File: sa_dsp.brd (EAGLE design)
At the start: 150 x 110 mm, 409 parts, among them CN1 uSD, CN2 MINI B USB, CN3 2X5 HEADER, CN4 MINI B USB, CN5 USB A, CN6 MINI B USB, Q1 2N7002, Q2 2N7002, Q3 2N7002, Q4 2N7002, SW1 1825910-7, U1 PGA2311, U10 LME49720, U11 PGA2311, U12 LME49720, U13 LME49720, U14 PCM1754, U15 LME49720, U16 PGA2311, U17 LME49720, U18 LME49720, U19 PCM1754, U2 LM317, U20 LME49720, U21 7 SEG, U22 74HC164A, U23 PCM2707, U24 PCM2707, U25 7 SEG, U26 74HC164A, U27 LM337, U28 LM317, U29 7 SEG, U3 OSD3358-512M-BSM, U30 74HC164A, U31 100MHz, U32 USBLC6-2SC6, U33 FT230X, U34 USBLC6-2SC6, U35 USBLC6-2SC6, U36 USBLC6-2SC6, U37 2 PORT HUB, U38 TPS70925, U39 LM22670, U4 LME49720, U40 MPM3820, U41 MPM3820, U5 LME49720, U6 10CL016YF484C6G, U7 7 SEG, U8 74HC164A, U9 PCM1754

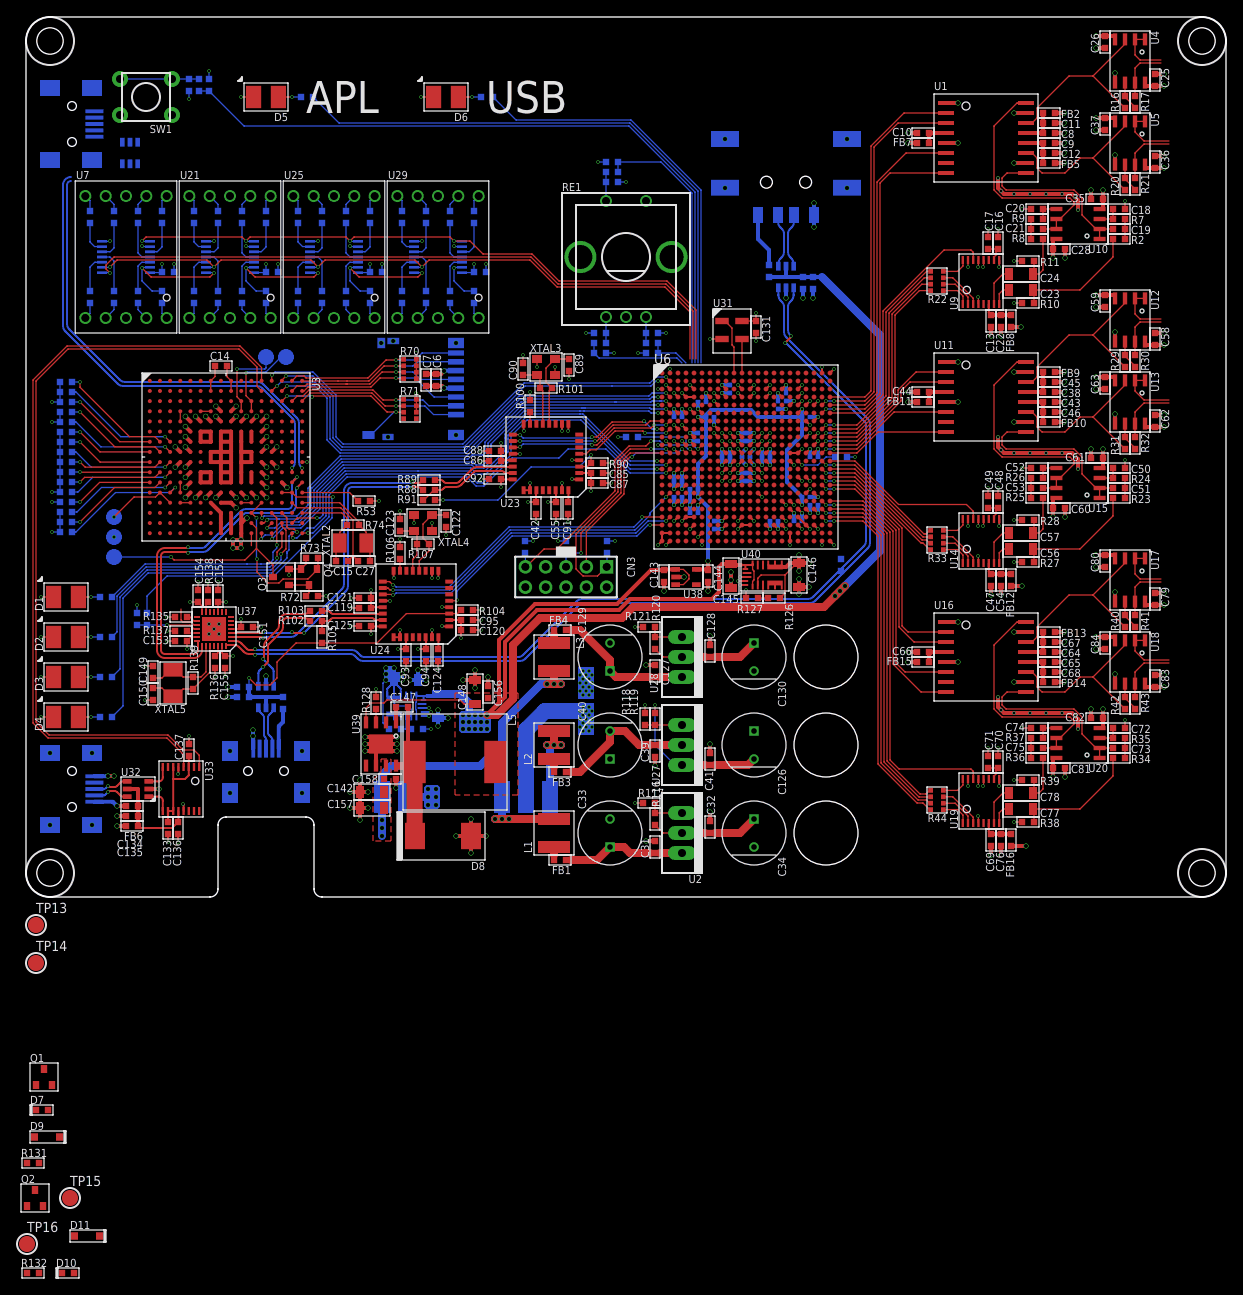
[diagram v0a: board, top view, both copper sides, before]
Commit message: FPGA config needs check, full review, DRC, airwires and architecture review needed
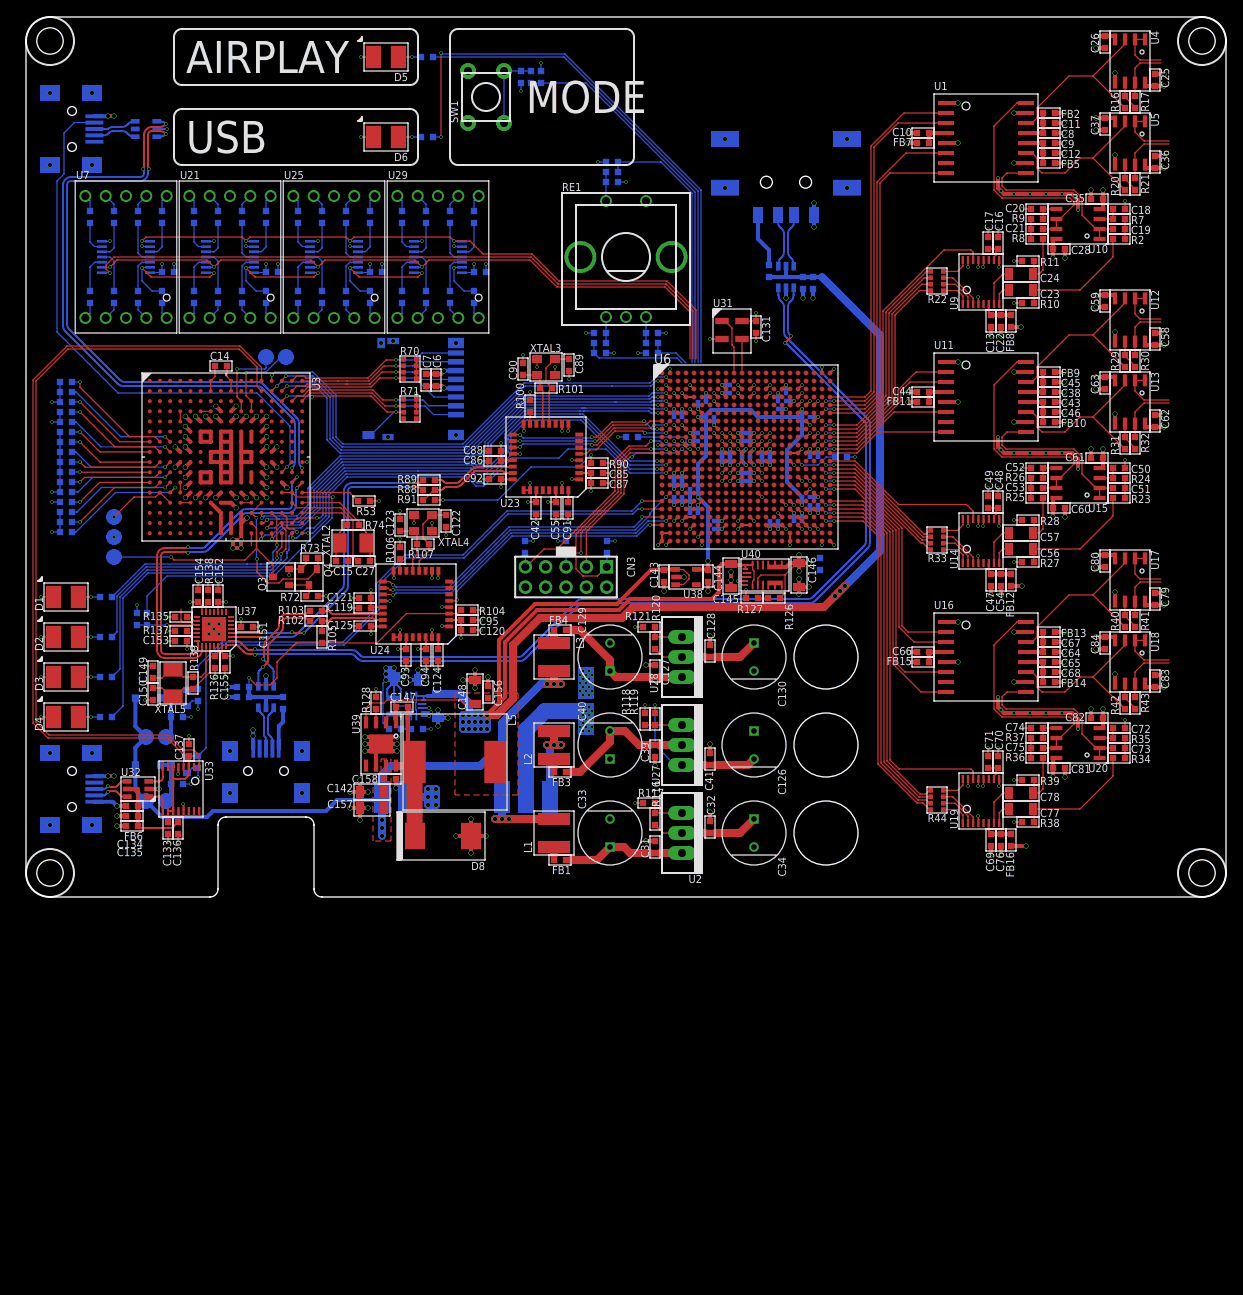
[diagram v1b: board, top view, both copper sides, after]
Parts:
- moved R132 75.1 mm to (21.5, 25.2), flipped to the bottom, turned to 90 degrees
- moved D10 70.8 mm to (18.9, 22.5), flipped to the bottom, turned to 180 degrees
- moved D11 67.7 mm to (15.2, 24.9), flipped to the bottom
- moved TP16 65.7 mm to (17.5, 20.0), flipped to the bottom, turned to 270 degrees
- moved Q2 65.0 mm to (19.1, 24.9), flipped to the bottom, turned to 270 degrees
- moved TP15 58.4 mm to (15.0, 20.0), flipped to the bottom, turned to 270 degrees
- moved R131 54.2 mm to (21.5, 16.9), flipped to the bottom, turned to 90 degrees
- moved D9 48.2 mm to (15.2, 16.5), flipped to the bottom
- moved D7 44.1 mm to (18.9, 14.1), flipped to the bottom, turned to 180 degrees
- moved SW1 42.5 mm to (57.5, 100.0), turned to 90 degrees
- moved Q1 42.5 mm to (19.1, 16.5), flipped to the bottom, turned to 270 degrees
- moved C132 41.5 mm to (64.4, 102.5)
- moved R122 41.5 mm to (61.9, 102.5)
- moved R123 41.5 mm to (63.1, 102.5)
- moved TP14 26.0 mm to (17.5, 12.0), flipped to the bottom, turned to 270 degrees
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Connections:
- net IO_AUDIO_RLY_EN: now also U6.U1
- net PSU_AMP_PWR_EN: now also U6.V1
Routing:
- net PSU_AMP_PWR_EN: track 0.00 -> 80.3 mm, vias 0 -> 1
- net IO_AUDIO_RLY_EN: track 0.00 -> 72.7 mm, vias 0 -> 1
- net OSD_DEBUG_USB_ID: track 0.00 -> 69.8 mm, vias 0 -> 1
- net 15VD_UNREG: track 39.6 -> 85.5 mm
- net UI_INPUT_SEL: track 88.6 -> 47.5 mm
- net UI_INPUT_USB: track 52.4 -> 72.7 mm, vias 0 -> 2
- net OSD_DEBUG_USB_DM: track 58.6 -> 77.3 mm, vias 1 -> 3
- net OSD_DEBUG_USB_DP: track 59.4 -> 78.0 mm, vias 1 -> 3
- net UI_INPUT_AIRPLAY: track 74.5 -> 61.6 mm
- net GND: track 337.1 -> 349.0 mm, vias 315 -> 326
- net N$237: track 0.00 -> 6.43 mm
- net N$207: track 0.00 -> 6.06 mm
- net N$209: track 0.00 -> 5.37 mm
- net N$208: track 0.00 -> 5.31 mm
- net 3V3: track 153.7 -> 154.9 mm
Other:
- board text added: "AIRPLAY"
- board text added: "MODE"
- board text removed: "APL"

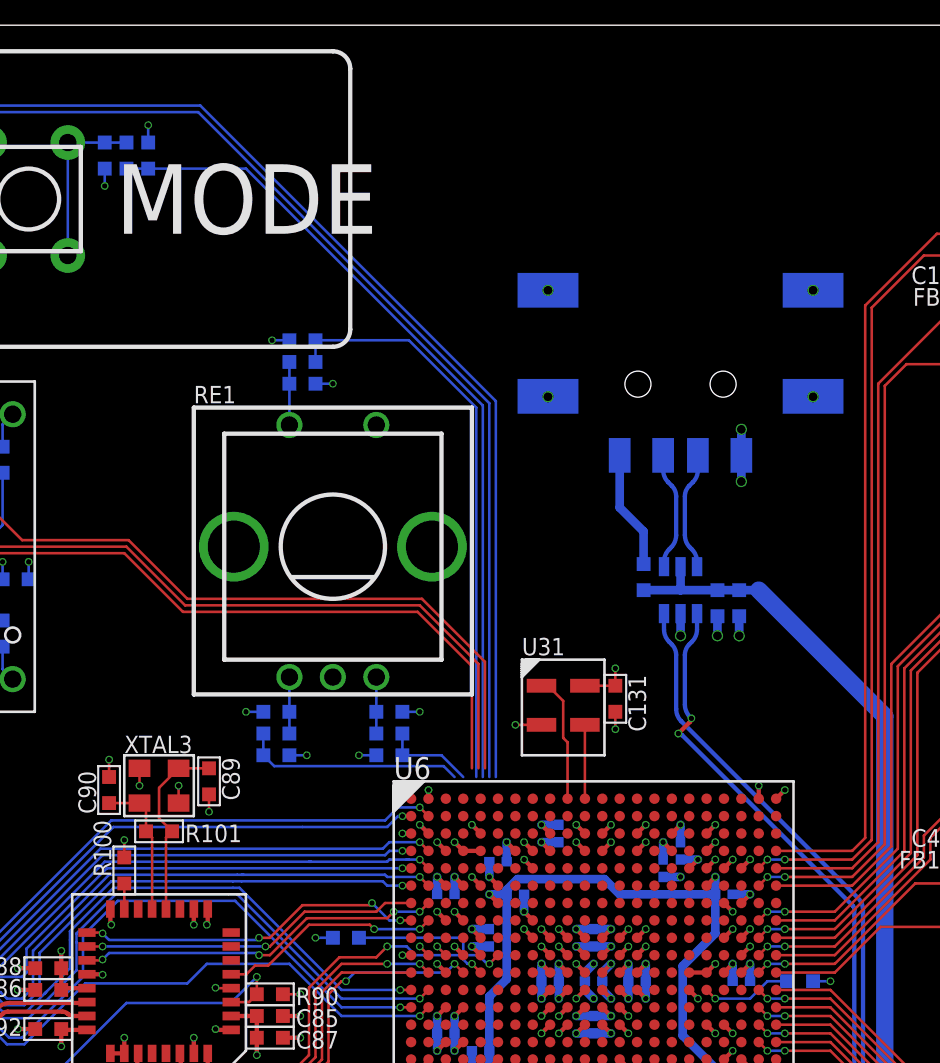
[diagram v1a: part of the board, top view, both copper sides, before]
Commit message: Schmit triggers done, FPGA conf done
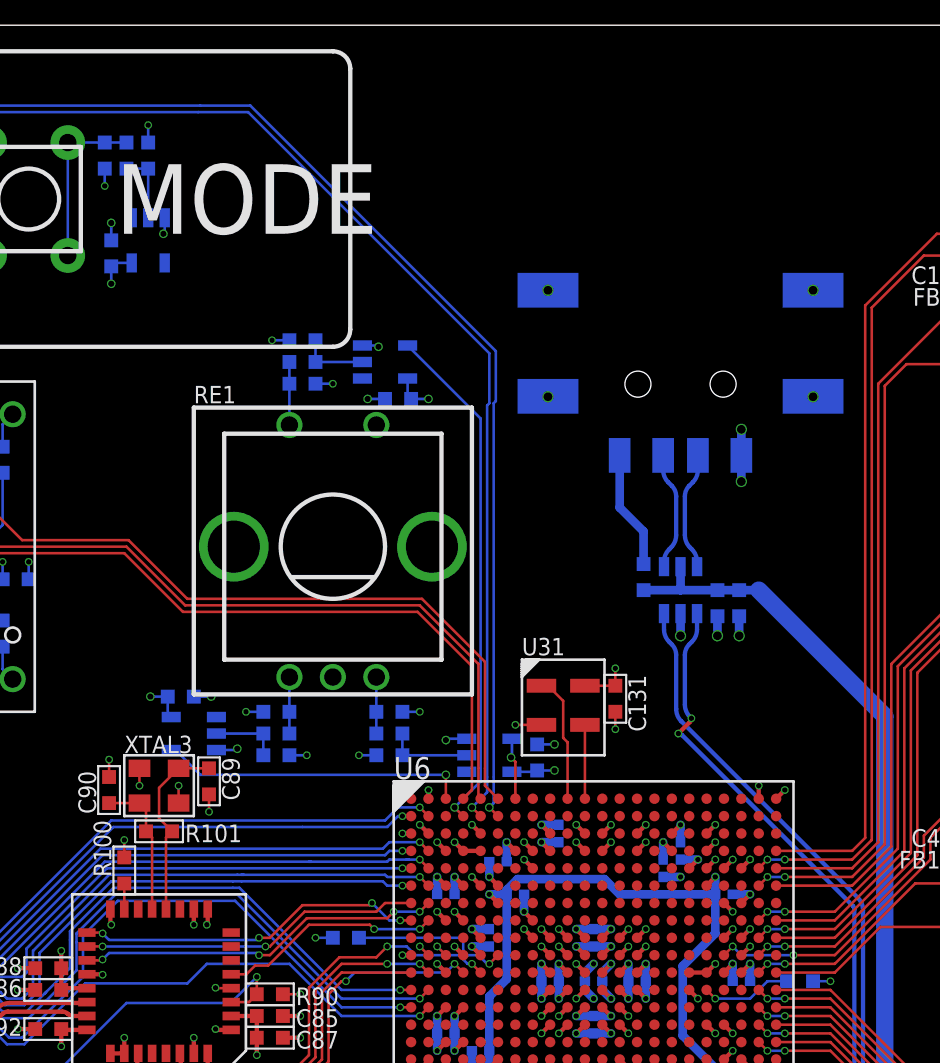
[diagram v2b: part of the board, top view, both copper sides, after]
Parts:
- added C161, C162, C163, C164: 100nF 16V, CAPACITORS:0603
- added U42, U43, U44, U45: SN74LVC1G17D, ICs:SOT23-5
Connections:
- new net N$238: C4.2, R5.2, U43.2
- new net N$239: C1.2, R4.2, U42.2
- new net N$240: C29.2, R13.1, U44.2
- new net N$241: C132.2, R123.2, U45.2
- net 3V3: now also C161.2, C162.2, C163.2, C164.2, U42.5, U43.5, U44.5, U45.5
- net DISP_SPI_!CE: now also U6.A4
- net DISP_SPI_MOSI: now also U6.A5
- net DISP_SPI_SCLK: now also U6.A6
- net ENC_A: now also U42.4, U6.A3; no longer C1.2, R4.2
- net ENC_B: now also U43.4, U6.A7; no longer C4.2, R5.2
- net ENC_SW: now also U44.4, U6.B4; no longer C29.2, R13.1
- net GND: now also C161.1, C162.1, C163.1, C164.1, U42.3, U43.3, U44.3, U45.3
- net PGA1_SDI: now also U6.K19; no longer U6.K22
- net UI_INPUT_AIRPLAY: now also U6.B5
- net UI_INPUT_SEL: now also U45.4; no longer C132.2, R123.2
- net UI_INPUT_USB: now also U6.B6
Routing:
- net UI_INPUT_SEL: track 47.5 -> 0.00 mm
- net 3V3: track 154.9 -> 164.1 mm, vias 82 -> 86
- net GND: track 349.0 -> 357.3 mm, vias 326 -> 334
- net ENC_A: track 12.8 -> 17.8 mm, vias 0 -> 1
- net N$238: track 0.00 -> 4.95 mm
- net UI_INPUT_AIRPLAY: track 61.6 -> 66.1 mm, vias 0 -> 1
- net UI_INPUT_USB: track 72.7 -> 77.0 mm, vias 2 -> 3
- net N$241: track 0.00 -> 4.08 mm
- net N$240: track 0.00 -> 3.95 mm
- net N$239: track 0.00 -> 3.95 mm
- net ENC_SW: track 33.4 -> 29.6 mm, vias 0 -> 1
- net PGA1_SDI: track 18.5 -> 21.9 mm, vias 0 -> 2
- net DISP_SPI_SCLK: track 84.3 -> 86.3 mm
- net DISP_SPI_!CE: track 87.7 -> 89.6 mm
- net DISP_SPI_MOSI: track 84.8 -> 86.6 mm
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
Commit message: Passes DRC
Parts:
- removed R87: 10k, r_0603:0603
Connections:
- removed net CONF_NCONFIG: R87.1
- net 3V3: no longer R87.2
- net AM_PWR_BTN: now also U6.R2
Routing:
- net AM_PWR_BTN: track 1.55 -> 71.3 mm, vias 0 -> 4
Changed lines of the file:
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@@
 <attribute name="PRICE_PER" value="0.10000" x="95.125" y="49.25" size="1.778" layer="28" rot="MR180" display="off"/>
 </element>
-<element name="R87" library="r_0603" package="0603" value="10k" x="99.25" y="41.625" smashed="yes" rot="MR90">
-<attribute name="DIGIKEY" value="P10.0KHCT-ND" x="101.75" y="31.375" size="1.778" layer="28" rot="MR90" display="off"/>
-<attribute name="FARNELL" value="" x="101.75" y="31.375" size="1.778" layer="28" rot="MR90" display="off"/>
-<attribute name="NAME" x="100" y="40.125" size="1.016" layer="26" rot="MR90"/>
-<attribute name="PRICE_PER" value="0.10000" x="101.75" y="31.375" size="1.778" layer="28" rot="MR90" display="off"/>
-</element>
 <element name="C96" library="CAPACITORS" package="0402" value="100nF 16V" x="97.5" y="60" smashed="yes" rot="MR0">
 <attribute name="DIGIKEY" value="1276-1001-6-ND" x="97.5" y="60" size="1.778" layer="28" rot="MR0" display="off"/>
@@
 <contactref element="R85" pad="2"/>
 <contactref element="R86" pad="2"/>
-<contactref element="R87" pad="2"/>
 <contactref element="U6" pad="K5"/>
 <contactref element="U6" pad="D11"/>
@@
 <wire x1="65.5" y1="71.375" x2="64.5" y2="71.375" width="0.1524" layer="16"/>
 <via x="64.5" y="71.375" extent="1-16" drill="0.35"/>
-<wire x1="99.5" y1="44" x2="99.25" y2="42.375" width="0" layer="19" extent="16-16"/>
 </signal>
 <signal name="+5V">
@@
 <wire x1="134.875" y1="32.5" x2="133.75" y2="32.5" width="0.5" layer="1"/>
 <via x="133.75" y="32.5" extent="1-16" drill="0.5"/>
-<wire x1="129.75" y1="98" x2="126.5" y2="94.75" width="1" layer="3"/>
-<wire x1="126.5" y1="94.75" x2="126.5" y2="89.375" width="1" layer="3"/>
+<wire x1="129.75" y1="98" x2="129.25" y2="98" width="1" layer="3"/>
+<wire x1="129.25" y1="98" x2="126.5" y2="95.25" width="1" layer="3"/>
+<wire x1="126.5" y1="95.25" x2="126.5" y2="89.375" width="1" layer="3"/>
 <wire x1="126.5" y1="89.375" x2="126.5" y2="75.25" width="1" layer="3"/>
 <wire x1="126.5" y1="65.75" x2="126.5" y2="57.375" width="1" layer="3"/>
@@
 <wire x1="28.175" y1="45.475" x2="28.175" y2="44" width="0.15" layer="1"/>
 <wire x1="28.175" y1="44" x2="28.175" y2="43.925" width="0.15" layer="1"/>
+<via x="28.175" y="43.925" extent="1-16" drill="0.3"/>
+<wire x1="28.175" y1="43.925" x2="28.175" y2="42.325" width="0.15" layer="16"/>
+<wire x1="28.175" y1="42.325" x2="28.25" y2="42.25" width="0.15" layer="16"/>
+<via x="28.25" y="42.25" extent="1-16" drill="0.3"/>
+<wire x1="28.25" y1="42.25" x2="28.25" y2="39.75" width="0.15" layer="1"/>
+<wire x1="45" y1="47.625" x2="46.125" y2="48.75" width="0.15" layer="1"/>
+<wire x1="58" y1="48.75" x2="60.875" y2="45.875" width="0.15" layer="1"/>
+<wire x1="60.875" y1="45.875" x2="68.25" y2="45.875" width="0.15" layer="1"/>
+<wire x1="71.25" y1="48.875" x2="71.25" y2="49.125" width="0.15" layer="1"/>
+<via x="71.25" y="49.125" extent="1-16" drill="0.3"/>
+<wire x1="28.25" y1="39.75" x2="31" y2="37" width="0.15" layer="1"/>
+<wire x1="31" y1="37" x2="38.875" y2="37" width="0.15" layer="1"/>
+<wire x1="38.875" y1="37" x2="42" y2="40.125" width="0.15" layer="1"/>
+<wire x1="42" y1="40.125" x2="43.625" y2="40.125" width="0.15" layer="1"/>
+<wire x1="43.625" y1="40.125" x2="45" y2="41.5" width="0.15" layer="1"/>
+<wire x1="45" y1="41.5" x2="45" y2="47.625" width="0.15" layer="1"/>
+<wire x1="46.125" y1="48.75" x2="58" y2="48.75" width="0.15" layer="1"/>
+<wire x1="68.25" y1="45.875" x2="71.25" y2="48.875" width="0.15" layer="1"/>
+<wire x1="71.25" y1="49.125" x2="73.125" y2="51" width="0.15" layer="16"/>
+<wire x1="73.125" y1="51" x2="80" y2="51" width="0.15" layer="16"/>
+<via x="80" y="51" extent="1-16" drill="0.3"/>
+<contactref element="U6" pad="R2"/>
+<wire x1="80.5" y1="51.5" x2="80" y2="51" width="0.15" layer="1"/>
 </signal>
 <signal name="N$153">
@@
 <wire x1="85.25" y1="48.75" x2="85.25" y2="42" width="0.5" layer="16"/>
 </signal>
-<signal name="CONF_NCONFIG">
-<contactref element="R87" pad="1"/>
-</signal>
 <signal name="CONF_NSTATUS">
 <contactref element="R85" pad="1"/>
@@
 <contactref element="C40" pad="N"/>
 <wire x1="67.5" y1="15.625" x2="68.125" y2="15.625" width="0.5" layer="1"/>
-<wire x1="73" y1="20.75" x2="73" y2="19.375" width="1" layer="1"/>
-<wire x1="73" y1="19.375" x2="69.25" y2="15.625" width="1" layer="1"/>
-<wire x1="69.25" y1="15.625" x2="68.125" y2="15.625" width="1" layer="1"/>
+<wire x1="73" y1="20.75" x2="73" y2="19.625" width="1" layer="1"/>
+<wire x1="73" y1="19.625" x2="69" y2="15.625" width="1" layer="1"/>
+<wire x1="69" y1="15.625" x2="68.125" y2="15.625" width="1" layer="1"/>
 <wire x1="78" y1="19" x2="78.625" y2="19" width="0.5" layer="1"/>
 <wire x1="79.25" y1="19" x2="78.625" y2="19" width="0.5" layer="1"/>
@@
 <via x="27.625" y="47.375" extent="1-16" drill="0.5"/>
 <wire x1="27.625" y1="47.375" x2="28.625" y2="48.375" width="0.5" layer="3"/>
-<wire x1="33" y1="48.375" x2="35.125" y2="50.5" width="0.5" layer="3"/>
-<wire x1="35.125" y1="50.5" x2="35.125" y2="54.375" width="0.5" layer="3"/>
+<wire x1="33" y1="48.375" x2="35.25" y2="50.625" width="0.5" layer="3"/>
+<wire x1="35.25" y1="54.25" x2="35.25" y2="50.625" width="0.5" layer="3"/>
+<wire x1="35.25" y1="54.25" x2="35.125" y2="54.375" width="0.5" layer="3"/>
 <wire x1="28.625" y1="48.375" x2="33" y2="48.375" width="0.5" layer="3"/>
 <wire x1="35.125" y1="54.375" x2="42.125" y2="54.375" width="0.5" layer="3"/>
@@
 <signal name="UI_INPUT_AIRPLAY">
 <contactref element="R124" pad="1"/>
-<wire x1="83.875" y1="88.125" x2="83.875" y2="66.75" width="0.15" layer="16"/>
-<wire x1="83.875" y1="88.125" x2="84" y2="88.25" width="0.15" layer="16"/>
-<wire x1="84" y1="88.25" x2="84" y2="91.125" width="0.15" layer="16"/>
+<wire x1="83.875" y1="88.375" x2="83.875" y2="66.75" width="0.15" layer="16"/>
+<wire x1="83.875" y1="88.375" x2="84" y2="88.5" width="0.15" layer="16"/>
+<wire x1="84" y1="88.5" x2="84" y2="91.125" width="0.15" layer="16"/>
 <wire x1="84" y1="91.125" x2="70.125" y2="105" width="0.15" layer="16"/>
 <wire x1="70.125" y1="105" x2="67.25" y2="105" width="0.15" layer="16"/>
@@
 <wire x1="31.625" y1="47.25" x2="30.25" y2="47.25" width="0.15" layer="16"/>
 <wire x1="30.25" y1="47.25" x2="30.125" y2="47.125" width="0.15" layer="16"/>
-<wire x1="34" y1="47.25" x2="35.625" y2="48.875" width="0.15" layer="16"/>
-<wire x1="35.625" y1="48.875" x2="35.625" y2="51.125" width="0.15" layer="16"/>
-<wire x1="35.625" y1="51.125" x2="35.625" y2="51.25" width="0.15" layer="16"/>
-<wire x1="34" y1="47.25" x2="31.625" y2="47.25" width="0.15" layer="16"/>
-<wire x1="35.625" y1="51.125" x2="35.75" y2="51.125" width="0.15" layer="16"/>
-<wire x1="35.75" y1="51.125" x2="39.375" y2="54.75" width="0.15" layer="16"/>
+<wire x1="31.625" y1="47.25" x2="34" y2="47.25" width="0.15" layer="16"/>
+<wire x1="36.25" y1="51.625" x2="39.375" y2="54.75" width="0.15" layer="16"/>
 <wire x1="55.25" y1="54.75" x2="55.75" y2="55.25" width="0.15" layer="16"/>
 <wire x1="55.75" y1="55.25" x2="57.125" y2="55.25" width="0.15" layer="16"/>
@@
 <via x="79" y="61.5" extent="1-16" drill="0.3"/>
 <wire x1="62" y1="61.5" x2="79" y2="61.5" width="0.15" layer="16"/>
+<wire x1="36.25" y1="51.625" x2="35.625" y2="51" width="0.15" layer="16"/>
+<wire x1="35.625" y1="50.875" x2="35.625" y2="51" width="0.15" layer="16"/>
+<wire x1="35.625" y1="48.875" x2="35.625" y2="50.875" width="0.15" layer="16"/>
+<wire x1="34" y1="47.25" x2="35.625" y2="48.875" width="0.15" layer="16"/>
 </signal>
 <signal name="OSD_FPGA_GPIO0">
@@
 <mfgpreviewcolor name="substratecolor" color="0xFF786E46"/>
 </mfgpreviewcolors>
+<errors>
+</errors>
 </board>
 </drawing>
